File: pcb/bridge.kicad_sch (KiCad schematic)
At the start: 50 parts, among them Q4 IRFR4105, Q5 BC817, Q6 IRFR4105, Q7 BC817, Q8 IRFR4105, Q9 IRFR4105, U1 74HC04, U10 LM75B, U2 74HC04

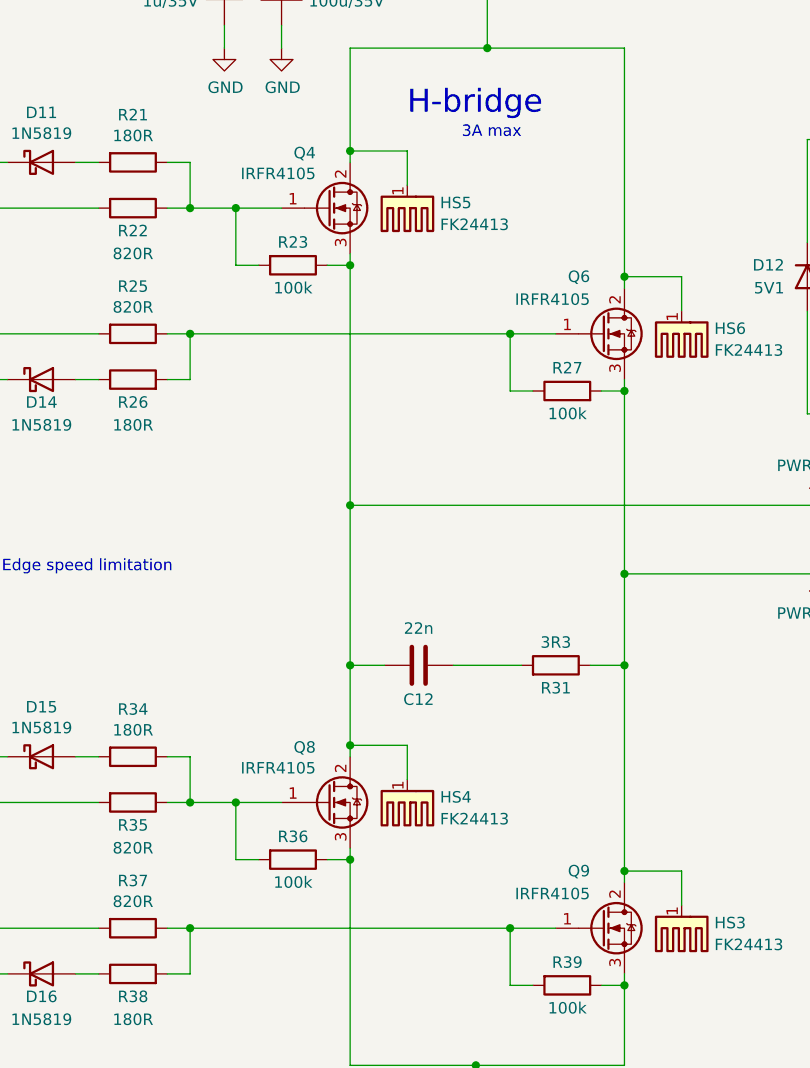
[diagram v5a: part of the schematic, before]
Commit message: Bridge: use IRLR2905 transistors instead of IRFR4105.
IRFR4105 seem not to be available.
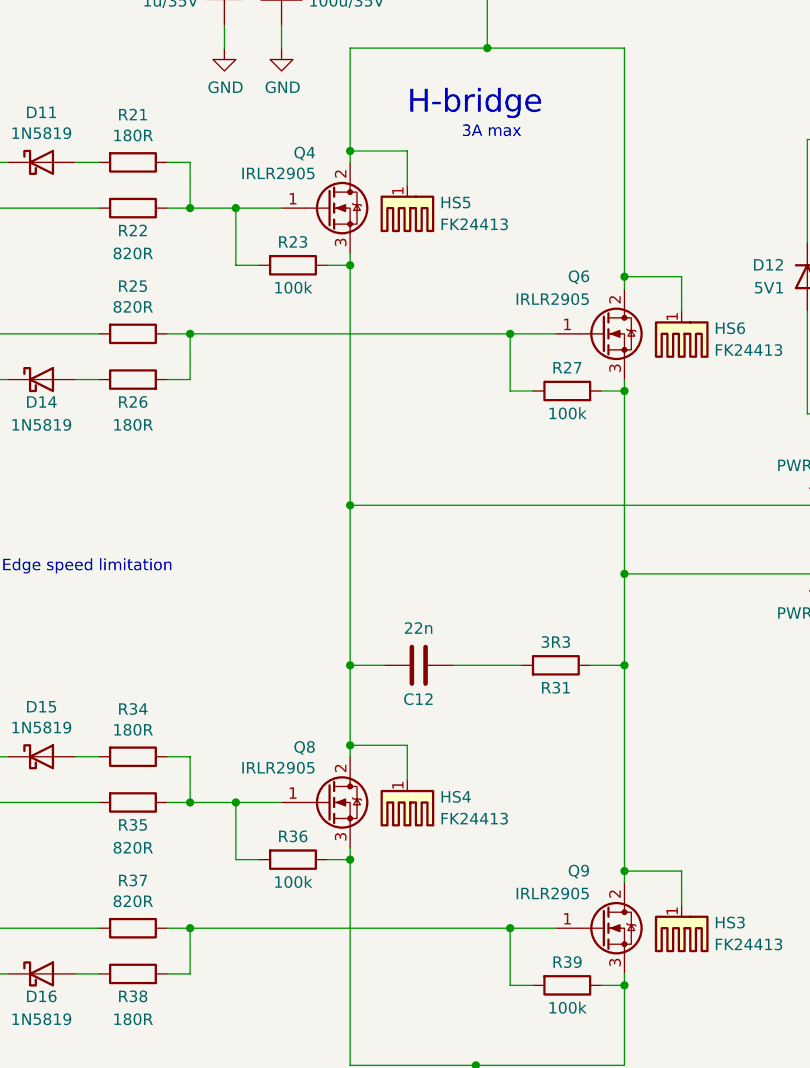
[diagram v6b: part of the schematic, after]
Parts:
- Q4, Q6, Q8, Q9: value IRFR4105 -> IRLR2905
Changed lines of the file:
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@@
 			)
 		)
-		(property "Value" "IRFR4105"
+		(property "Value" "IRLR2905"
 			(at 163.83 120.65 0)
 			(effects
@@
 			)
 		)
-		(property "Value" "IRFR4105"
+		(property "Value" "IRLR2905"
 			(at 163.83 54.61 0)
 			(effects
@@
 			)
 		)
-		(property "Value" "IRFR4105"
+		(property "Value" "IRLR2905"
 			(at 194.31 68.58 0)
 			(effects
@@
 			)
 		)
-		(property "Value" "IRFR4105"
+		(property "Value" "IRLR2905"
 			(at 194.31 134.62 0)
 			(effects

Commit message: Add F5 missing footprint.
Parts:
- HS3, HS4, HS5, HS6: footprint (none) -> Heatsink:Heatsink_Fischer_FK24413DPAK_23x13mm
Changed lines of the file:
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@@
 			)
 		)
-		(property "Footprint" ""
+		(property "Footprint" "Heatsink:Heatsink_Fischer_FK24413DPAK_23x13mm"
 			(at 204.1652 137.16 0)
 			(effects
@@
 			)
 		)
-		(property "Footprint" ""
+		(property "Footprint" "Heatsink:Heatsink_Fischer_FK24413DPAK_23x13mm"
 			(at 204.1652 71.12 0)
 			(effects
@@
 			)
 		)
-		(property "Footprint" ""
+		(property "Footprint" "Heatsink:Heatsink_Fischer_FK24413DPAK_23x13mm"
 			(at 173.6852 123.19 0)
 			(effects
@@
 			)
 		)
-		(property "Footprint" ""
+		(property "Footprint" "Heatsink:Heatsink_Fischer_FK24413DPAK_23x13mm"
 			(at 173.6852 57.15 0)
 			(effects

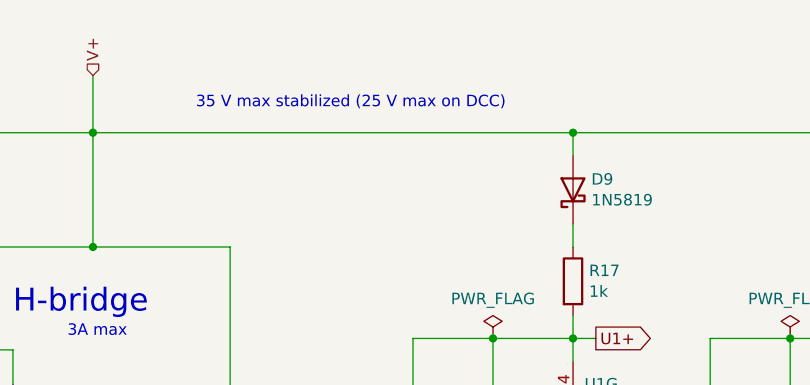
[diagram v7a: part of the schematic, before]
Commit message: Use switched power supply for 5V internal.
78M05 would have 2.5 W of heat loss on it @ 30V input.
Other minor improvements.
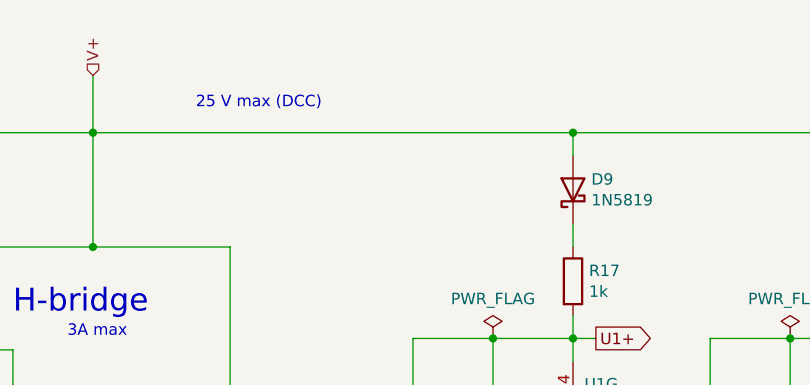
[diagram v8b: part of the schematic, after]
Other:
- note added: "25 V max (DCC)"
- note removed: "35 V max stabilized (25 V max on DCC)"
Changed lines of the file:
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@@
 		)
 	)
-	(text "35 V max stabilized (25 V max on DCC)"
+	(text "25 V max (DCC)"
 		(exclude_from_sim no)
 		(at 194.31 25.4 0)
